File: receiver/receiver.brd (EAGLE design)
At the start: 45.5 x 24.2 mm, 10 parts, among them P1 PROMICRO_HEADER, P2 PROMICRO_HEADER, U1 CORE51822B, U2 AZ1117IH

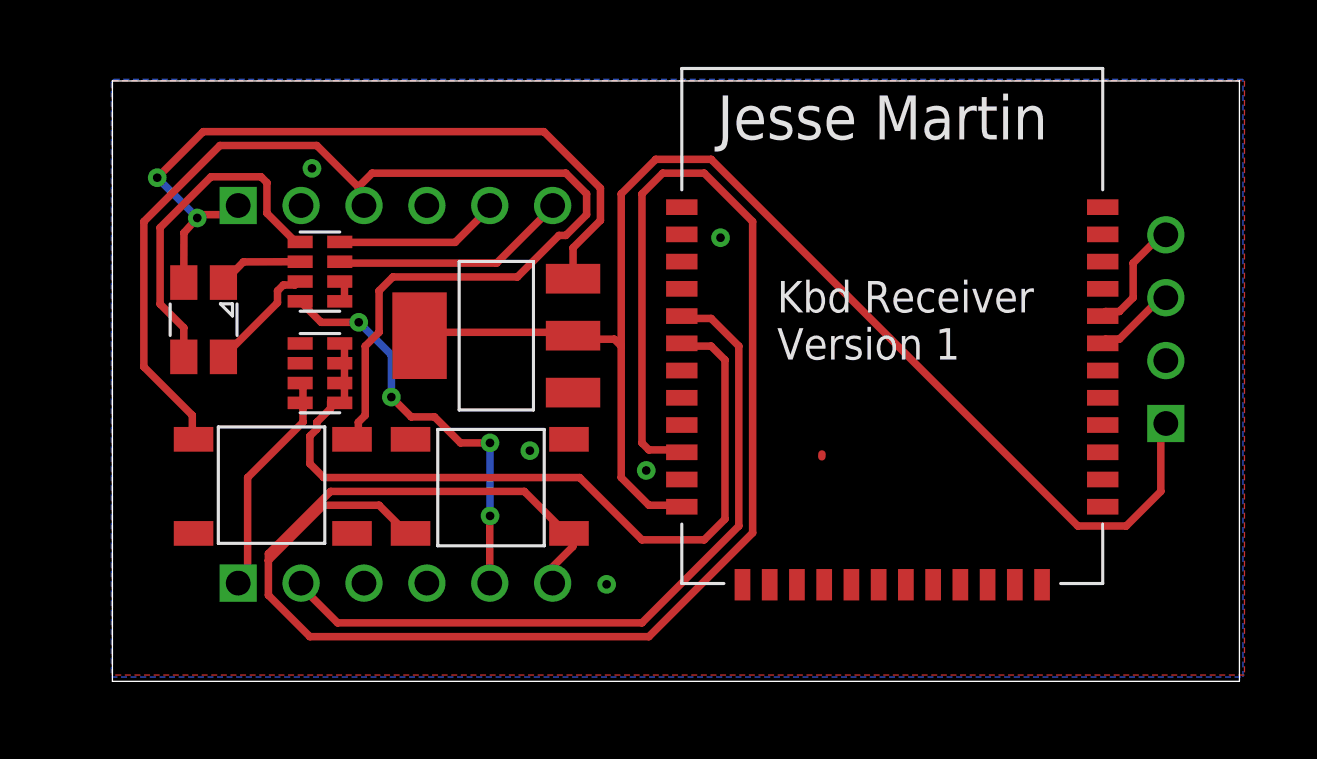
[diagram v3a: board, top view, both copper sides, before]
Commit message: reposition prog header
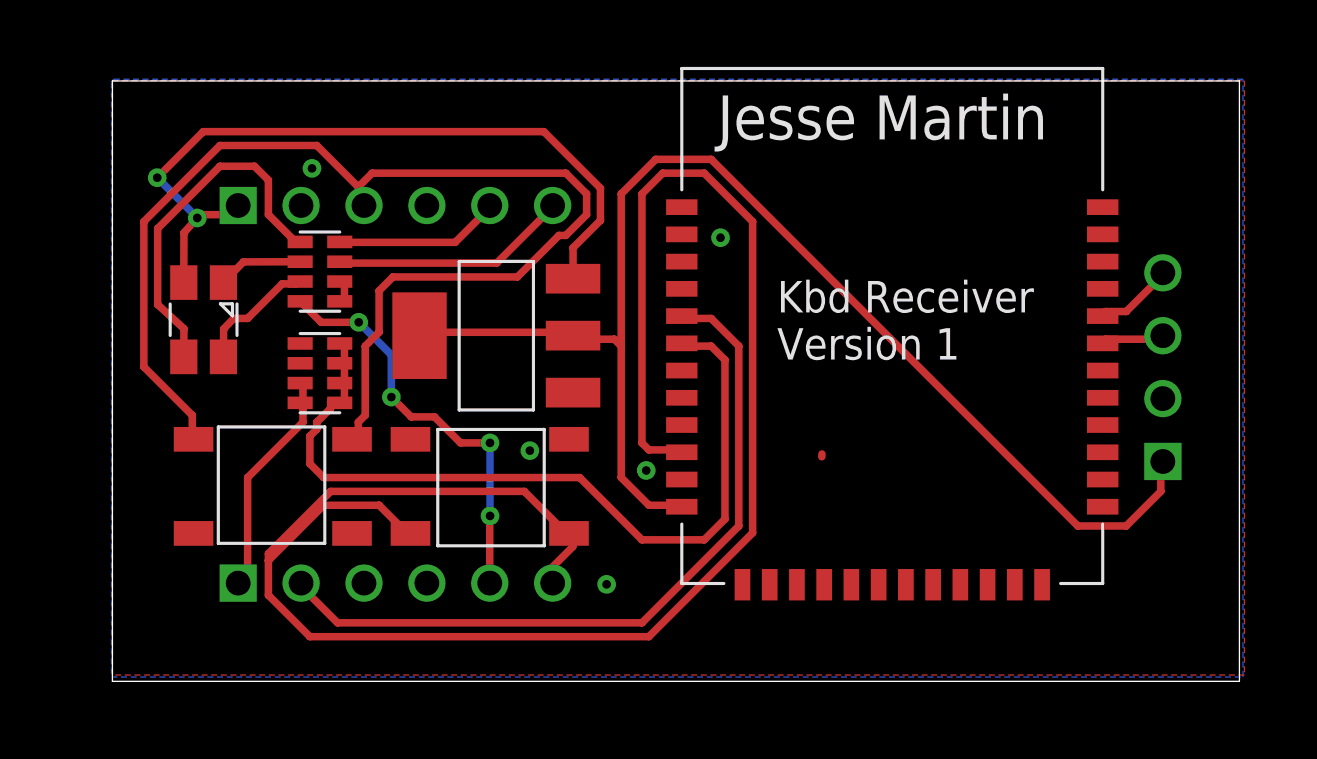
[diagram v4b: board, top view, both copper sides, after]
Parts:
- moved U$1 1.54 mm to (83.1, 50.7)
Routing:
- net VCC: track 54.8 -> 53.2 mm
- net SWCLK: track 4.75 -> 3.22 mm
- net SWDIO: track 3.33 -> 2.60 mm
- net N$14: track 13.9 -> 14.5 mm
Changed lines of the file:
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@@
 <layer number="20" name="Dimension" color="24" fill="1" visible="yes" active="yes"/>
 <layer number="21" name="tPlace" color="7" fill="1" visible="yes" active="yes"/>
-<layer number="22" name="bPlace" color="7" fill="1" visible="no" active="yes"/>
+<layer number="22" name="bPlace" color="7" fill="1" visible="yes" active="yes"/>
 <layer number="23" name="tOrigins" color="15" fill="1" visible="yes" active="yes"/>
-<layer number="24" name="bOrigins" color="15" fill="1" visible="no" active="yes"/>
+<layer number="24" name="bOrigins" color="15" fill="1" visible="yes" active="yes"/>
 <layer number="25" name="tNames" color="7" fill="1" visible="yes" active="yes"/>
-<layer number="26" name="bNames" color="7" fill="1" visible="no" active="yes"/>
-<layer number="27" name="tValues" color="7" fill="1" visible="no" active="yes"/>
-<layer number="28" name="bValues" color="7" fill="1" visible="no" active="yes"/>
+<layer number="26" name="bNames" color="7" fill="1" visible="yes" active="yes"/>
+<layer number="27" name="tValues" color="7" fill="1" visible="yes" active="yes"/>
+<layer number="28" name="bValues" color="7" fill="1" visible="yes" active="yes"/>
 <layer number="29" name="tStop" color="7" fill="3" visible="no" active="yes"/>
 <layer number="30" name="bStop" color="7" fill="6" visible="no" active="yes"/>
@@
 <layer number="38" name="bTest" color="7" fill="1" visible="no" active="yes"/>
 <layer number="39" name="tKeepout" color="4" fill="11" visible="yes" active="yes"/>
-<layer number="40" name="bKeepout" color="1" fill="11" visible="no" active="yes"/>
+<layer number="40" name="bKeepout" color="1" fill="11" visible="yes" active="yes"/>
 <layer number="41" name="tRestrict" color="4" fill="10" visible="yes" active="yes"/>
-<layer number="42" name="bRestrict" color="1" fill="10" visible="no" active="yes"/>
+<layer number="42" name="bRestrict" color="1" fill="10" visible="yes" active="yes"/>
 <layer number="43" name="vRestrict" color="2" fill="10" visible="no" active="yes"/>
-<layer number="44" name="Drills" color="7" fill="1" visible="no" active="yes"/>
+<layer number="44" name="Drills" color="7" fill="1" visible="yes" active="yes"/>
 <layer number="45" name="Holes" color="7" fill="1" visible="yes" active="yes"/>
 <layer number="46" name="Milling" color="3" fill="1" visible="no" active="yes"/>
@@
 <layer number="50" name="dxf" color="7" fill="1" visible="no" active="no"/>
 <layer number="51" name="tDocu" color="7" fill="1" visible="yes" active="yes"/>
-<layer number="52" name="bDocu" color="7" fill="1" visible="no" active="yes"/>
+<layer number="52" name="bDocu" color="7" fill="1" visible="yes" active="yes"/>
 <layer number="53" name="tGND_GNDA" color="7" fill="9" visible="no" active="no"/>
 <layer number="54" name="bGND_GNDA" color="1" fill="9" visible="no" active="no"/>
@@
 <element name="P1" library="promicro_header" package="PROMICRO_HEADER" value="PROMICRO_HEADER" x="52.07" y="45.75" smashed="yes" rot="R90"/>
 <element name="U2" library="az1117ih" package="AZ1117IH" value="AZ1117IH" x="56.144" y="55.743" rot="R90"/>
-<element name="U$1" library="prog_header" package="PROG_HEADER" value="PROG_HEADER" x="83.185" y="52.197" rot="R180"/>
+<element name="U$1" library="prog_header" package="PROG_HEADER" value="PROG_HEADER" x="83.064740625" y="50.66245625" rot="R180"/>
 </elements>
 <signals>
@@
 <wire x1="59.2328" y1="55.88" x2="59.244" y2="55.743" width="0.3048" layer="1"/>
 <contactref element="U$1" pad="VCC"/>
-<wire x1="82.9818" y1="49.4538" x2="82.9818" y2="51.9684" width="0.3048" layer="1"/>
-<wire x1="81.5848" y1="48.0568" x2="82.9818" y2="49.4538" width="0.3048" layer="1"/>
-<wire x1="79.629" y1="48.0568" x2="81.5848" y2="48.0568" width="0.3048" layer="1"/>
 <wire x1="64.8208" y1="62.865" x2="79.629" y2="48.0568" width="0.3048" layer="1"/>
 <wire x1="62.5856" y1="62.865" x2="64.8208" y2="62.865" width="0.3048" layer="1"/>
 <wire x1="61.1886" y1="61.468" x2="62.5856" y2="62.865" width="0.3048" layer="1"/>
 <wire x1="61.1886" y1="55.3212" x2="61.1886" y2="61.468" width="0.3048" layer="1"/>
-<wire x1="82.9818" y1="51.9684" x2="83.185" y2="52.197" width="0.3048" layer="1"/>
+<wire x1="82.9818" y1="49.4538" x2="82.9818" y2="50.5714" width="0.3048" layer="1"/>
+<wire x1="81.5848" y1="48.0568" x2="82.9818" y2="49.4538" width="0.3048" layer="1"/>
+<wire x1="79.629" y1="48.0568" x2="81.5848" y2="48.0568" width="0.3048" layer="1"/>
+<wire x1="82.9818" y1="50.5714" x2="83.064740625" y2="50.66245625" width="0.3048" layer="1"/>
 </signal>
 <signal name="LED-G">
@@
 <contactref element="D1" pad="GREEN"/>
 <contactref element="RA1" pad="P$7"/>
+<wire x1="47.498" y1="57.8358" x2="48.0568" y2="57.8358" width="0.3048" layer="1"/>
+<wire x1="46.101" y1="56.4388" x2="47.498" y2="57.8358" width="0.3048" layer="1"/>
+<wire x1="45.5422" y1="56.4388" x2="46.101" y2="56.4388" width="0.3048" layer="1"/>
+<wire x1="45.5422" y1="56.4388" x2="45.13231875" y2="56.014375" width="0.3048" layer="1"/>
 <wire x1="48.0568" y1="57.8358" x2="48.222" y2="57.929659375" width="0.3048" layer="1"/>
-<wire x1="47.3076" y1="57.0726" x2="47.3076" y2="57.55199375" width="0.3048" layer="1"/>
-<wire x1="47.3076" y1="57.55199375" x2="47.5456625" y2="57.79005625" width="0.3048" layer="1"/>
-<wire x1="47.5456625" y1="57.79005625" x2="48.01105625" y2="57.79005625" width="0.3048" layer="1"/>
-<wire x1="48.01105625" y1="57.79005625" x2="48.0568" y2="57.8358" width="0.3048" layer="1"/>
-<wire x1="45.123" y1="54.888" x2="47.3076" y2="57.0726" width="0.3048" layer="1"/>
+<wire x1="45.13231875" y1="56.014375" x2="45.123" y2="54.888" width="0.3048" layer="1"/>
 </signal>
 <signal name="N$14">
 <contactref element="D1" pad="BLUE"/>
 <contactref element="RA1" pad="P$5"/>
+<wire x1="46.9392" y1="60.6298" x2="48.0568" y2="59.5122" width="0.3048" layer="1"/>
+<wire x1="46.9392" y1="62.0268" x2="46.9392" y2="60.6298" width="0.3048" layer="1"/>
+<wire x1="46.3804" y1="62.5856" x2="46.9392" y2="62.0268" width="0.3048" layer="1"/>
+<wire x1="44.9834" y1="62.5856" x2="46.3804" y2="62.5856" width="0.3048" layer="1"/>
+<wire x1="42.4688" y1="60.071" x2="44.9834" y2="62.5856" width="0.3048" layer="1"/>
+<wire x1="42.4688" y1="56.9976" x2="42.4688" y2="60.071" width="0.3048" layer="1"/>
+<wire x1="42.4688" y1="56.9976" x2="43.528409375" y2="56.025025" width="0.3048" layer="1"/>
 <wire x1="48.0568" y1="59.5122" x2="48.222" y2="59.529659375" width="0.3048" layer="1"/>
-<wire x1="46.6423375" y1="62.1604" x2="46.8804" y2="61.9223375" width="0.3048" layer="1"/>
-<wire x1="42.5666" y1="57.0196625" x2="42.5666" y2="60.10571875" width="0.3048" layer="1"/>
-<wire x1="42.5666" y1="60.10571875" x2="44.62128125" y2="62.1604" width="0.3048" layer="1"/>
-<wire x1="44.62128125" y1="62.1604" x2="46.6423375" y2="62.1604" width="0.3048" layer="1"/>
-<wire x1="46.8804" y1="61.9223375" x2="46.8804" y2="60.6886" width="0.3048" layer="1"/>
-<wire x1="46.8804" y1="60.6886" x2="48.0568" y2="59.5122" width="0.3048" layer="1"/>
-<wire x1="43.523" y1="56.0632625" x2="42.5666" y2="57.0196625" width="0.3048" layer="1"/>
-<wire x1="43.523" y1="54.888" x2="43.523" y2="56.0632625" width="0.3048" layer="1"/>
+<wire x1="43.528409375" y1="56.025025" x2="43.523" y2="54.888" width="0.3048" layer="1"/>
 </signal>
 <signal name="RESET">
@@
 <contactref element="U1" pad="SWCLK"/>
 <contactref element="U$1" pad="SWCLK"/>
-<wire x1="81.3054" y1="56.7182" x2="80.7466" y2="56.7182" width="0.3048" layer="1"/>
-<wire x1="81.8642" y1="57.277" x2="81.3054" y2="56.7182" width="0.3048" layer="1"/>
-<wire x1="81.8642" y1="58.674" x2="81.8642" y2="57.277" width="0.3048" layer="1"/>
-<wire x1="82.9818" y1="59.7916" x2="81.8642" y2="58.674" width="0.3048" layer="1"/>
+<wire x1="81.5848" y1="56.7182" x2="80.7466" y2="56.7182" width="0.3048" layer="1"/>
+<wire x1="82.9818" y1="58.1152" x2="81.5848" y2="56.7182" width="0.3048" layer="1"/>
 <wire x1="80.7466" y1="56.7182" x2="80.636" y2="56.534" width="0.3048" layer="1"/>
-<wire x1="82.9818" y1="59.7916" x2="83.185" y2="59.817" width="0.3048" layer="1"/>
+<wire x1="82.9818" y1="58.1152" x2="83.064740625" y2="58.28245625" width="0.3048" layer="1"/>
 </signal>
 <signal name="SWDIO">
 <contactref element="U$1" pad="SWDIO"/>
 <contactref element="U1" pad="SWDIO"/>
-<wire x1="81.3054" y1="55.6006" x2="80.7466" y2="55.6006" width="0.3048" layer="1"/>
-<wire x1="82.9818" y1="57.277" x2="81.3054" y2="55.6006" width="0.3048" layer="1"/>
+<wire x1="82.9818" y1="55.6006" x2="80.7466" y2="55.6006" width="0.3048" layer="1"/>
 <wire x1="80.7466" y1="55.6006" x2="80.636" y2="55.434" width="0.3048" layer="1"/>
-<wire x1="82.9818" y1="57.277" x2="83.185" y2="57.277" width="0.3048" layer="1"/>
+<wire x1="82.9818" y1="55.6006" x2="83.064740625" y2="55.74245625" width="0.3048" layer="1"/>
 </signal>
 <signal name="N$2">

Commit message: revise board layout
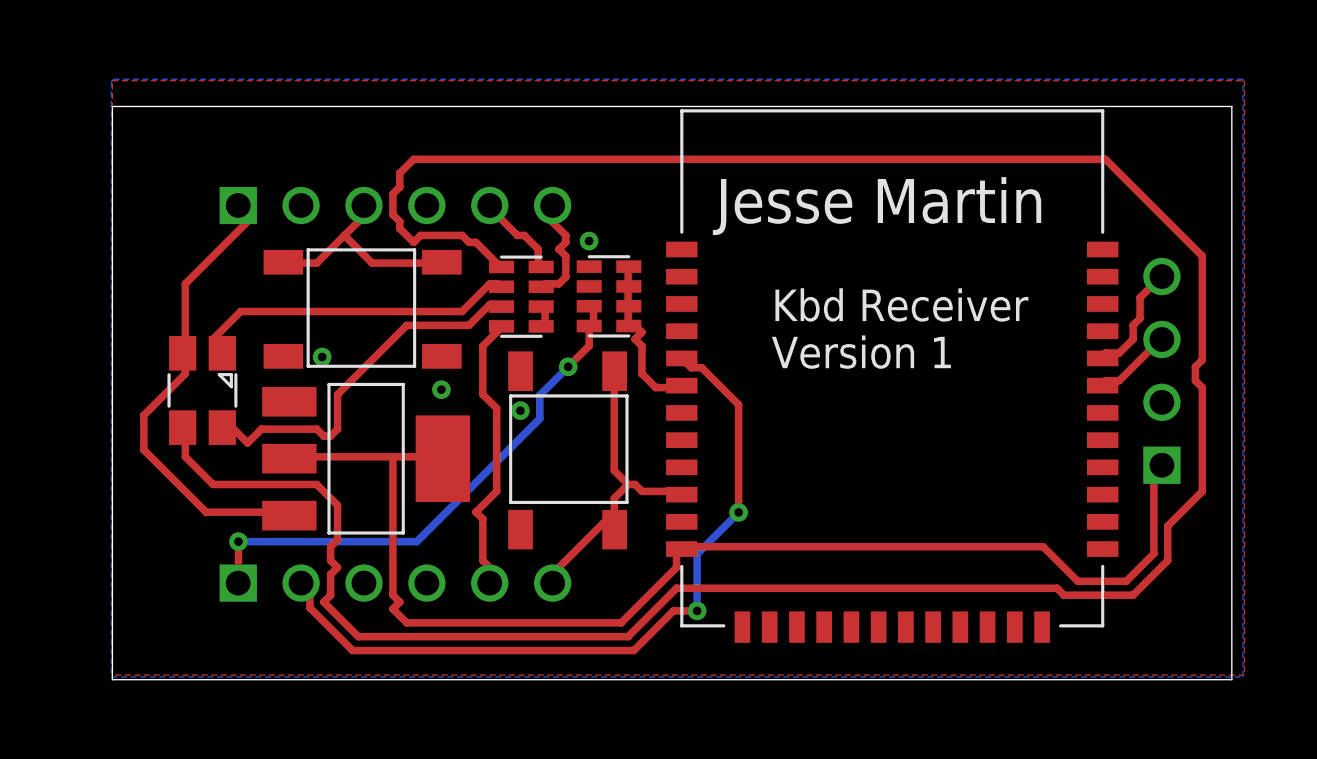
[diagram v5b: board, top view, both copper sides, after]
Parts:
- moved RA2 12.1 mm to (60.7, 57.3)
- moved RA1 8.20 mm to (57.2, 57.3)
- moved B2 8.02 mm to (50.7, 56.8)
- moved U2 7.23 mm to (50.9, 50.8), turned to 270 degrees
- moved B1 3.46 mm to (59.0, 51.1), turned to 90 degrees
- moved D1 2.86 mm to (44.3, 53.5)
- moved U1 1.71 mm to (72.1, 54.4)
- moved U$1 0.16 mm to (83.0, 50.5)
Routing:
- net N$14: track 14.5 -> 103.5 mm
- net PAIR: track 77.1 -> 13.9 mm
- net RESET: track 47.8 -> 8.94 mm
- net TXO-DIV: track 33.1 -> 6.84 mm
- net TXO: track 9.30 -> 21.5 mm, vias 0 -> 2
- net VIN: track 30.8 -> 18.9 mm, vias 2 -> 0
- net N$10: track 5.00 -> 15.1 mm
- net N$11: track 3.63 -> 13.4 mm
- net LED-G: track 16.7 -> 11.5 mm, vias 4 -> 0
- net LED-R: track 9.60 -> 4.50 mm
- net VCC: track 53.2 -> 49.9 mm
- net LED-B: track 6.73 -> 3.50 mm
- net SWCLK: track 3.22 -> 4.62 mm
- net SWDIO: track 2.60 -> 3.21 mm
- net RXI: track 30.1 -> 30.3 mm, vias 0 -> 2
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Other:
- board size 45.5 x 24.2 mm -> 45.2 x 23.1 mm
